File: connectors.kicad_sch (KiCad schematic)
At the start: 7 parts, among them J1 USB_C_Receptacle_USB2.0_14P, J2 Conn_01x04, J3 Conn_01x04, J4 Conn_01x02, J6 Conn_01x02

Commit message: Start routing antennna
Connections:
- net VBUS: no longer J3.2 (Pin_2)
- new net VDD: J3.2 (Pin_2)
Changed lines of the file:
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@@
+    )
+  )
+  (global_label "VDD" (shape input) (at 171.45 33.02 0) (fields_autoplaced)
+    (effects (font (size 1.27 1.27)) (justify left))
+    (property "Intersheetrefs" "${INTERSHEET_REFS}" (at 178.0638 33.02 0)
+      (effects (font (size 1.27 1.27)) (justify left) hide)
     )
   )
@@
       (effects (font (size 1.27 1.27)) (justify left) hide)
     )
-  )
-  (global_label "VBUS" (shape input) (at 171.45 33.02 0) (fields_autoplaced)
-    (effects (font (size 1.27 1.27)) (justify left))
-    (property "Intersheetrefs" "${INTERSHEET_REFS}" (at 179.3338 33.02 0)
-      (effects (font (size 1.27 1.27)) (justify left) hide)
-    )

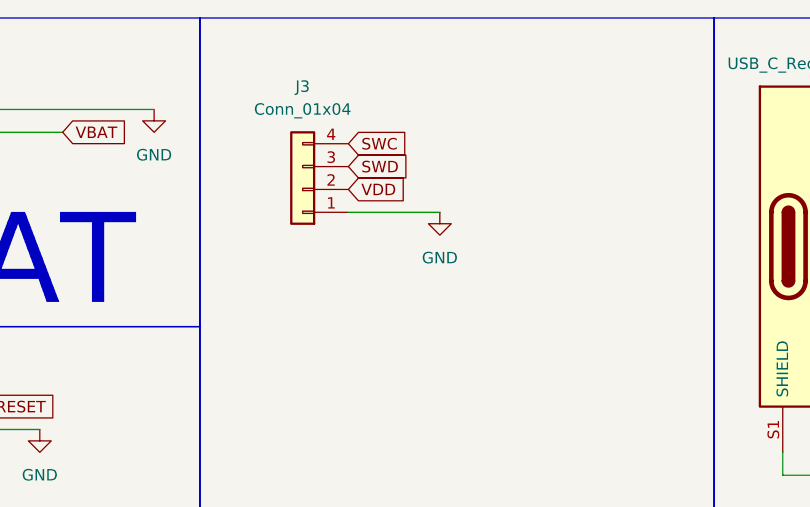
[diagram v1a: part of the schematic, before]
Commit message: Change board shape
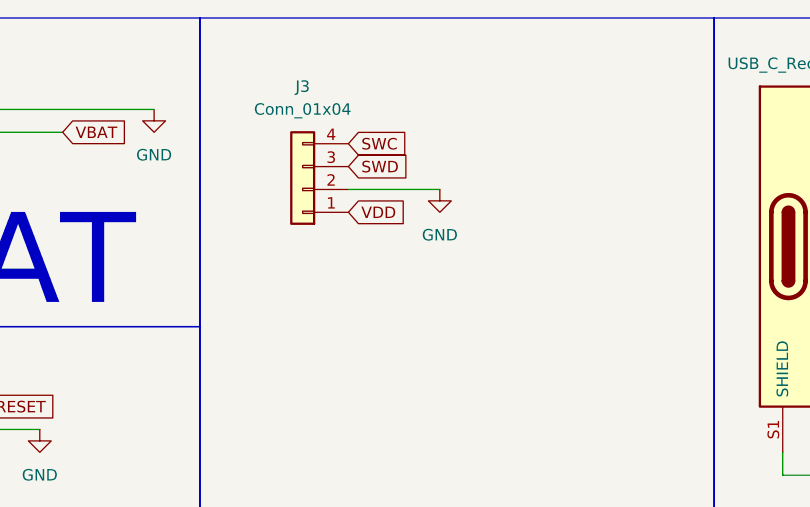
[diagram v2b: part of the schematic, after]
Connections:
- net GND: now also J3.2 (Pin_2); no longer J3.1 (Pin_1)
- net VDD: now also J3.1 (Pin_1); no longer J3.2 (Pin_2)
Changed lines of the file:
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@@
-    (stroke (width 0) (type default))
-  )
-  (wire (pts (xy 171.45 35.56) (xy 181.61 35.56))
     (stroke (width 0) (type default))
   )
@@
   )
   (wire (pts (xy 219.71 64.77) (xy 227.33 64.77))
+    (stroke (width 0) (type default))
+  )
+  (wire (pts (xy 171.45 33.02) (xy 181.61 33.02))
     (stroke (width 0) (type default))
   )
@@
     )
   )
+  (global_label "VDD" (shape input) (at 171.45 35.56 0) (fields_autoplaced)
+    (effects (font (size 1.27 1.27)) (justify left))
+    (property "Intersheetrefs" "${INTERSHEET_REFS}" (at 178.0638 35.56 0)
+      (effects (font (size 1.27 1.27)) (justify left) hide)
+    )
+  )
   (global_label "VBAT" (shape input) (at 139.7 26.67 0) (fields_autoplaced)
     (effects (font (size 1.27 1.27)) (justify left))
@@
     (effects (font (size 1.27 1.27)) (justify left))
     (property "Intersheetrefs" "${INTERSHEET_REFS}" (at 261.0976 54.61 0)
-      (effects (font (size 1.27 1.27)) (justify left) hide)
-    )
-  )
-  (global_label "VDD" (shape input) (at 171.45 33.02 0) (fields_autoplaced)
-    (effects (font (size 1.27 1.27)) (justify left))
-    (property "Intersheetrefs" "${INTERSHEET_REFS}" (at 178.0638 33.02 0)
       (effects (font (size 1.27 1.27)) (justify left) hide)
     )
@@
     )
   )
+  (symbol (lib_id "power:GND") (at 181.61 33.02 0) (unit 1)
+    (in_bom yes) (on_board yes) (dnp no) (fields_autoplaced)
+    (property "Reference" "#PWR014" (at 181.61 39.37 0)
+      (effects (font (size 1.27 1.27)) hide)
+    )
+    (property "Value" "GND" (at 181.61 38.1 0)
+      (effects (font (size 1.27 1.27)))
+    )
+    (property "Footprint" "" (at 181.61 33.02 0)
+      (effects (font (size 1.27 1.27)) hide)
+    )
+    (property "Datasheet" "" (at 181.61 33.02 0)
+      (effects (font (size 1.27 1.27)) hide)
+    )
+    (pin "1")
+    (instances
+      (project "keyboard"
+        (path "/a3795772-e8b2-4a24-8aa0-5a93e6e5ac56/4e5c1308-6948-4418-b24d-d3d63913e2f4"
+          (reference "#PWR014") (unit 1)
+        )
+      )
+    )
+  )
   (symbol (lib_id "power:GND") (at 227.33 67.31 0) (unit 1)
     (in_bom yes) (on_board yes) (dnp no) (fields_autoplaced)
@@
         )
       )
-    )
-  )
-  (symbol (lib_id "power:GND") (at 181.61 35.56 0) (unit 1)
-    (in_bom yes) (on_board yes) (dnp no) (fields_autoplaced)
-    (property "Reference" "#PWR014" (at 181.61 41.91 0)
-      (effects (font (size 1.27 1.27)) hide)
-    )
-    (property "Value" "GND" (at 181.61 40.64 0)
-      (effects (font (size 1.27 1.27)))
-    )
-    (property "Footprint" "" (at 181.61 35.56 0)
-      (effects (font (size 1.27 1.27)) hide)
-    )
-    (property "Datasheet" "" (at 181.61 35.56 0)
-      (effects (font (size 1.27 1.27)) hide)
-    )
-    (pin "1")
-    (instances
-      (project "keyboard"
-        (path "/a3795772-e8b2-4a24-8aa0-5a93e6e5ac56/4e5c1308-6948-4418-b24d-d3d63913e2f4"
-          (reference "#PWR014") (unit 1)
-        )
-      )
